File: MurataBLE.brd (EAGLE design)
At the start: 70 x 92 mm, 39 parts, among them CON1 C-2235, IC1 I-5448, IC3 74LVC1G00DBV, Q1 FC-135 32.7680KA-AG3, Q2 12MHz, SW1 P8073, SW2 P8073, SW3 P8073, U1 IC_BLE_LBCA2HNZYZ-711, X1 TSW-112-02-S-S

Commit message: [ USB ] lisence stated
CC-BY-SA
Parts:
- added TP5, TP6, TP7, TP8: TPTP06R, testpad_local:TP06R
- TP1, TP2, TP3, TP4: value TPTP07SQ -> TPTP06SQ; device testpad_local:TP07SQ -> testpad_local:TP06SQ
- moved TP1 0.30 mm to (42.2, 25.4)
- moved TP3 0.30 mm to (42.2, 26.7)
- moved TP2 0.20 mm to (43.0, 25.4)
- moved TP4 0.20 mm to (43.0, 26.7)
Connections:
- net P0_0: now also TP8.TP
- net P0_1: now also TP7.TP
- net TGT_RX: now also TP6.TP
- net TGT_TX: now also TP5.TP
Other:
- board text added: "CC-BY-SA Licensed"
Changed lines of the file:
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@@
 <wire x1="23.2" y1="28.8" x2="24.1" y2="28.8" width="0.15" layer="41"/>
 <wire x1="23.2" y1="27.6" x2="24.1" y2="27.6" width="0.15" layer="41"/>
+<text x="52.6" y="39.4" size="1" layer="16" ratio="20" rot="MR0">CC-BY-SA Licensed</text>
 </plain>
 <attributes>
@@
 <attribute name="VALUE" x="29.9" y="28.7" size="1" layer="27" ratio="20"/>
 </element>
-<element name="TP1" library="testpad_local" package="TP07SQ" value="TPTP07SQ" x="41.9" y="25.4" smashed="yes">
-<attribute name="TP_SIGNAL_NAME" value="" x="41.9" y="23.495" size="1" layer="37"/>
-<attribute name="VALUE" x="41.519" y="25.019" size="0.0254" layer="27"/>
-</element>
-<element name="TP2" library="testpad_local" package="TP07SQ" value="TPTP07SQ" x="42.8" y="25.4" smashed="yes">
-<attribute name="TP_SIGNAL_NAME" value="" x="42.8" y="23.495" size="1" layer="37"/>
-<attribute name="VALUE" x="42.419" y="25.019" size="0.0254" layer="27"/>
-</element>
-<element name="TP3" library="testpad_local" package="TP07SQ" value="TPTP07SQ" x="41.9" y="26.7" smashed="yes">
-<attribute name="TP_SIGNAL_NAME" value="" x="41.9" y="24.795" size="1" layer="37"/>
-<attribute name="VALUE" x="41.519" y="26.319" size="0.0254" layer="27"/>
-</element>
-<element name="TP4" library="testpad_local" package="TP07SQ" value="TPTP07SQ" x="42.8" y="26.7" smashed="yes">
-<attribute name="TP_SIGNAL_NAME" value="" x="42.8" y="24.795" size="1" layer="37"/>
-<attribute name="VALUE" x="42.419" y="26.319" size="0.0254" layer="27"/>
+<element name="TP1" library="testpad_local" package="TP06SQ" value="TPTP06SQ" x="42.2" y="25.4" smashed="yes">
+<attribute name="TP_SIGNAL_NAME" value="" x="42.2" y="23.495" size="1" layer="37"/>
+<attribute name="VALUE" x="41.819" y="25.019" size="0.0254" layer="27"/>
+</element>
+<element name="TP2" library="testpad_local" package="TP06SQ" value="TPTP06SQ" x="43" y="25.4" smashed="yes">
+<attribute name="TP_SIGNAL_NAME" value="" x="43" y="23.495" size="1" layer="37"/>
+<attribute name="VALUE" x="42.619" y="25.019" size="0.0254" layer="27"/>
+</element>
+<element name="TP3" library="testpad_local" package="TP06SQ" value="TPTP06SQ" x="42.2" y="26.7" smashed="yes">
+<attribute name="TP_SIGNAL_NAME" value="" x="42.2" y="24.795" size="1" layer="37"/>
+<attribute name="VALUE" x="41.819" y="26.319" size="0.0254" layer="27"/>
+</element>
+<element name="TP4" library="testpad_local" package="TP06SQ" value="TPTP06SQ" x="43" y="26.7" smashed="yes">
+<attribute name="TP_SIGNAL_NAME" value="" x="43" y="24.795" size="1" layer="37"/>
+<attribute name="VALUE" x="42.619" y="26.319" size="0.0254" layer="27"/>
 </element>
 <element name="R4" library="mylib" package="C0402" value="270/1005" x="32" y="27.3" smashed="yes" rot="R90">
@@
 <element name="LED1" library="mylib" package="LED_3SEG_SMD" value="LED_3SEG" x="22.4" y="35.8" smashed="yes">
 <attribute name="NAME" x="25.3" y="35.3" size="1" layer="25" ratio="20"/>
+</element>
+<element name="TP5" library="testpad_local" package="TP06R" value="TPTP06R" x="41.9" y="25.4" smashed="yes">
+<attribute name="TP_SIGNAL_NAME" value="" x="41.9" y="23.495" size="1" layer="37"/>
+<attribute name="VALUE" x="41.646" y="24.892" size="0.0254" layer="27"/>
+</element>
+<element name="TP6" library="testpad_local" package="TP06R" value="TPTP06R" x="41.9" y="26.7" smashed="yes">
+<attribute name="TP_SIGNAL_NAME" value="" x="41.9" y="24.795" size="1" layer="37"/>
+<attribute name="VALUE" x="41.646" y="26.192" size="0.0254" layer="27"/>
+</element>
+<element name="TP7" library="testpad_local" package="TP06R" value="TPTP06R" x="43.3" y="26.7" smashed="yes">
+<attribute name="TP_SIGNAL_NAME" value="" x="43.3" y="24.795" size="1" layer="37"/>
+<attribute name="VALUE" x="43.046" y="26.192" size="0.0254" layer="27"/>
+</element>
+<element name="TP8" library="testpad_local" package="TP06R" value="TPTP06R" x="43.3" y="25.4" smashed="yes">
+<attribute name="TP_SIGNAL_NAME" value="" x="43.3" y="23.495" size="1" layer="37"/>
+<attribute name="VALUE" x="43.046" y="24.892" size="0.0254" layer="27"/>
 </element>
 </elements>
@@
 <wire x1="48.7" y1="26" x2="48.7" y2="25.7" width="0.25" layer="1"/>
 <wire x1="48.7" y1="25.7" x2="45.8" y2="22.8" width="0.25" layer="1"/>
-<wire x1="43.7" y1="25.4" x2="44.3" y2="26" width="0.25" layer="1"/>
-<wire x1="44.3" y1="26" x2="48.7" y2="26" width="0.25" layer="1"/>
+<wire x1="44" y1="25.4" x2="44.6" y2="26" width="0.25" layer="1"/>
+<wire x1="44.6" y1="26" x2="48.7" y2="26" width="0.25" layer="1"/>
 <wire x1="45.8" y1="22.8" x2="45.8" y2="22.2" width="0.25" layer="1"/>
 <wire x1="33" y1="15.6" x2="39.2" y2="15.6" width="0.25" layer="1"/>
@@
 <wire x1="31.7" y1="14.3" x2="33" y2="15.6" width="0.25" layer="1"/>
 <contactref element="TP2" pad="TP"/>
-<wire x1="42.8" y1="25.4" x2="43.7" y2="25.4" width="0.25" layer="1"/>
+<contactref element="TP8" pad="TP"/>
+<wire x1="43" y1="25.4" x2="43.3" y2="25.4" width="0.25" layer="1"/>
+<wire x1="44" y1="25.4" x2="43.3" y2="25.4" width="0.25" layer="1"/>
 </signal>
 <signal name="P0_1">
@@
 <wire x1="31.4" y1="14.8" x2="32.7" y2="16.1" width="0.25" layer="1"/>
 <contactref element="TP4" pad="TP"/>
-<wire x1="48.7" y1="26.7" x2="42.8" y2="26.7" width="0.25" layer="1"/>
+<wire x1="48.7" y1="26.7" x2="43.3" y2="26.7" width="0.25" layer="1"/>
+<contactref element="TP7" pad="TP"/>
+<wire x1="43.3" y1="26.7" x2="43" y2="26.7" width="0.25" layer="1"/>
 </signal>
 <signal name="P0_2">
@@
 <wire x1="41.4" y1="23.7" x2="41.4" y2="24.9" width="0.25" layer="1"/>
 <contactref element="TP1" pad="TP"/>
-<wire x1="41.9" y1="25.4" x2="41.4" y2="24.9" width="0.25" layer="1"/>
+<contactref element="TP5" pad="TP"/>
+<wire x1="42.2" y1="25.4" x2="41.9" y2="25.4" width="0.25" layer="1"/>
+<wire x1="41.4" y1="24.9" x2="41.9" y2="25.4" width="0.25" layer="1"/>
 </signal>
 <signal name="TGT_RX">
@@
 <wire x1="40.25" y1="23.35" x2="40.9" y2="24" width="0.25" layer="1"/>
 <contactref element="TP3" pad="TP"/>
-<wire x1="41.9" y1="26.7" x2="40.9" y2="25.7" width="0.25" layer="1"/>
+<contactref element="TP6" pad="TP"/>
+<wire x1="42.2" y1="26.7" x2="41.9" y2="26.7" width="0.25" layer="1"/>
+<wire x1="40.9" y1="25.7" x2="41.9" y2="26.7" width="0.25" layer="1"/>
 </signal>
 <signal name="N$4">

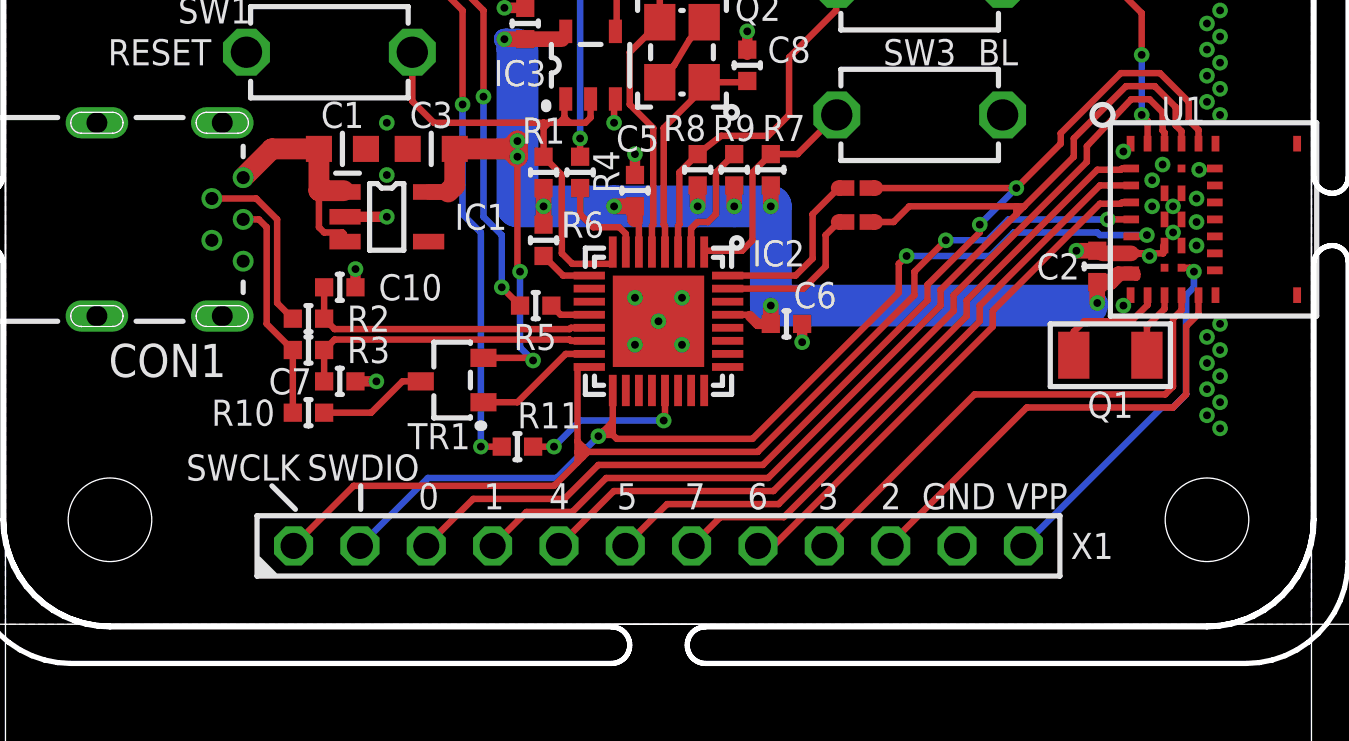
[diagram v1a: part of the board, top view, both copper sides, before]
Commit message: [ USB ] extend pin header X1
now ALL pins on header
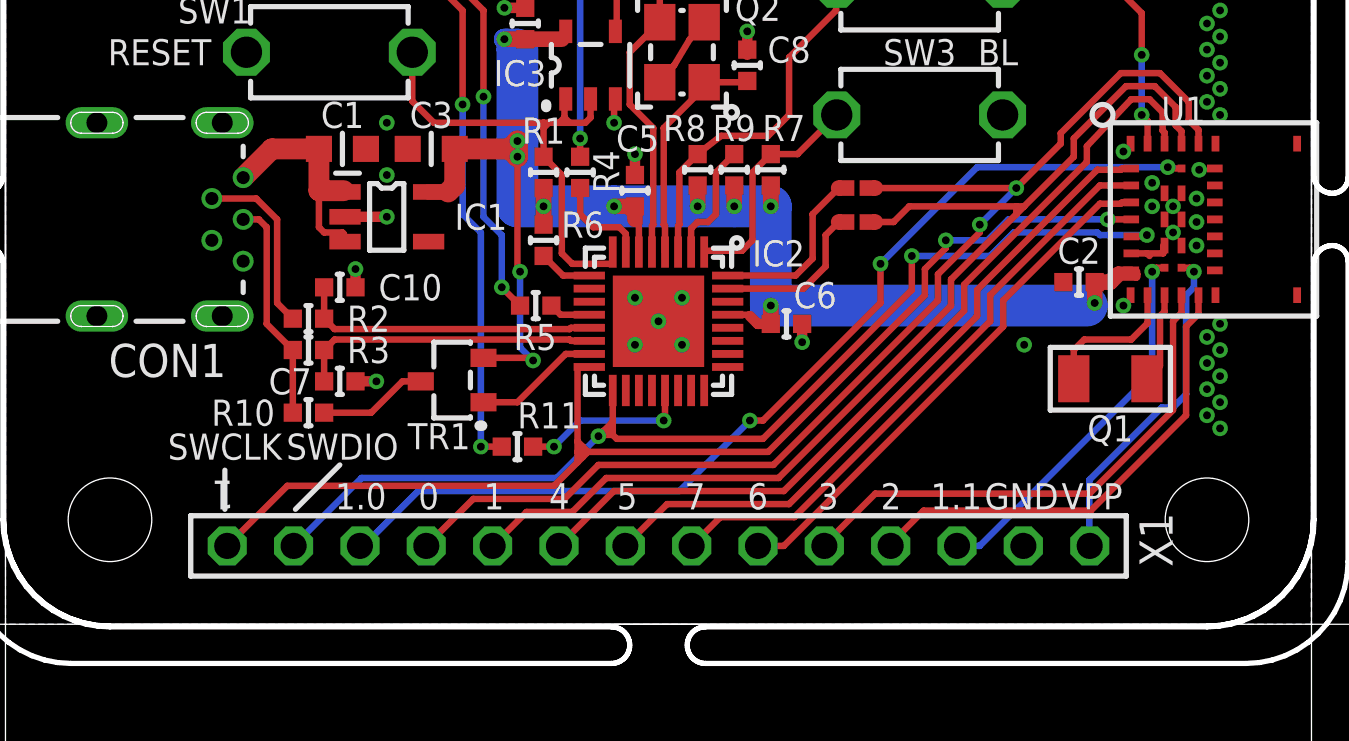
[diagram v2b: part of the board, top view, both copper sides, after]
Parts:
- X1: value TSW-112-02-S-S -> TSW-114-02-S-S; device con-samtec.local:TSW-112-02-S-S -> con-samtec.local:TSW-114-02-S-S
- moved C2 0.92 mm to (51.1, 23.1), turned to 180 degrees
- moved Q1 0.90 mm to (52.3, 19.4)
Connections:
- net GND: now also X1.13; no longer X1.11
- net P0_0: now also X1.5; no longer X1.4
- net P0_1: now also X1.4; no longer X1.3
- net P0_2: now also X1.11; no longer X1.10
- net P0_3: now also X1.10; no longer X1.9
- net P0_4: now also X1.6; no longer X1.5
- net P0_5: now also X1.7; no longer X1.6
- net P0_6: now also X1.9; no longer X1.8
- net P0_7: now also X1.8; no longer X1.7
- net P1_0: now also X1.3
- net P1_1: now also X1.12
- net VPP: now also X1.14; no longer X1.12
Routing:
- net P1_0: track 0.00 -> 38.4 mm, vias 0 -> 3
- net P1_1: track 0.00 -> 14.6 mm, vias 0 -> 1
- net SWCLK: track 43.2 -> 46.0 mm
- net SWDIO: track 39.5 -> 42.2 mm
- net GND: track 24.2 -> 21.7 mm, vias 48 -> 46
- net VPP: track 14.0 -> 13.0 mm
- net N$2: track 4.52 -> 5.42 mm
- net N$3: track 2.58 -> 3.48 mm
- net P0_3: track 19.5 -> 20.1 mm
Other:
- board text added: "1.0"
- board text added: "1.1"

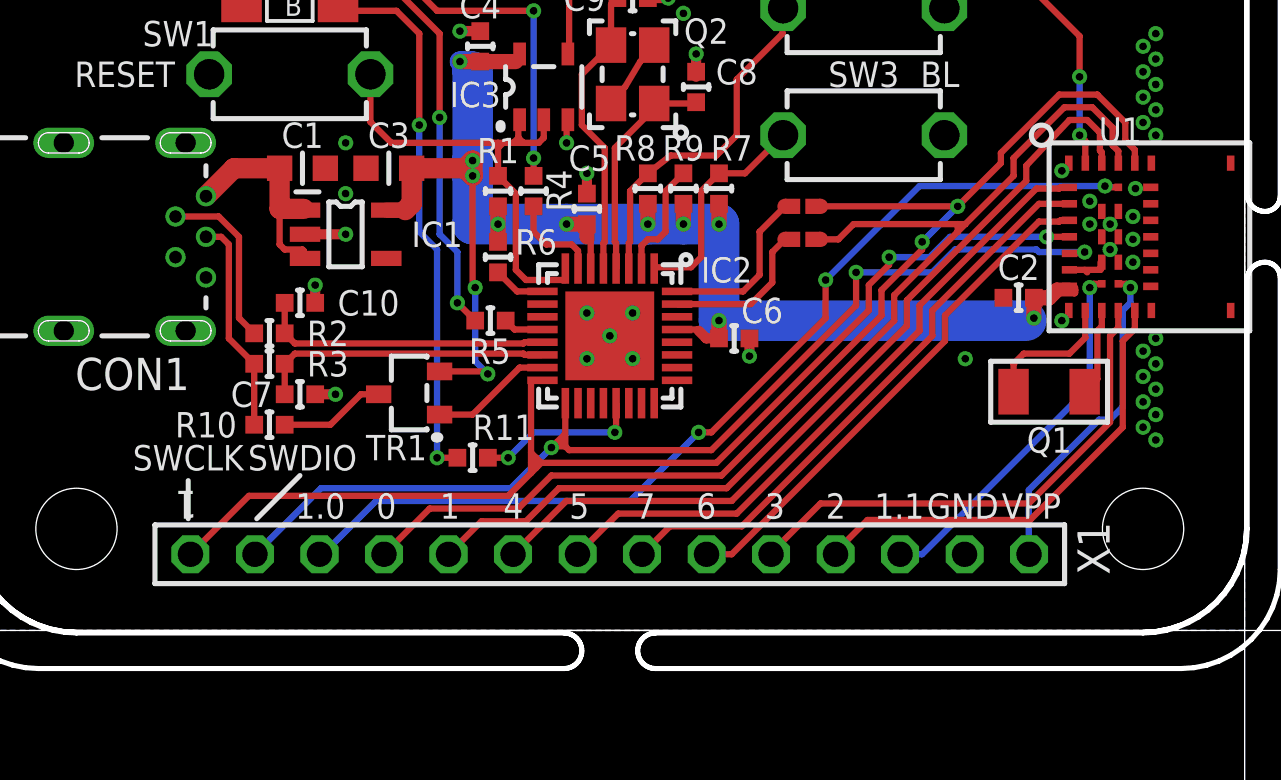
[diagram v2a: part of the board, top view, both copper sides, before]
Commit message: [ USB ] update as library
TP
X1 Pin header
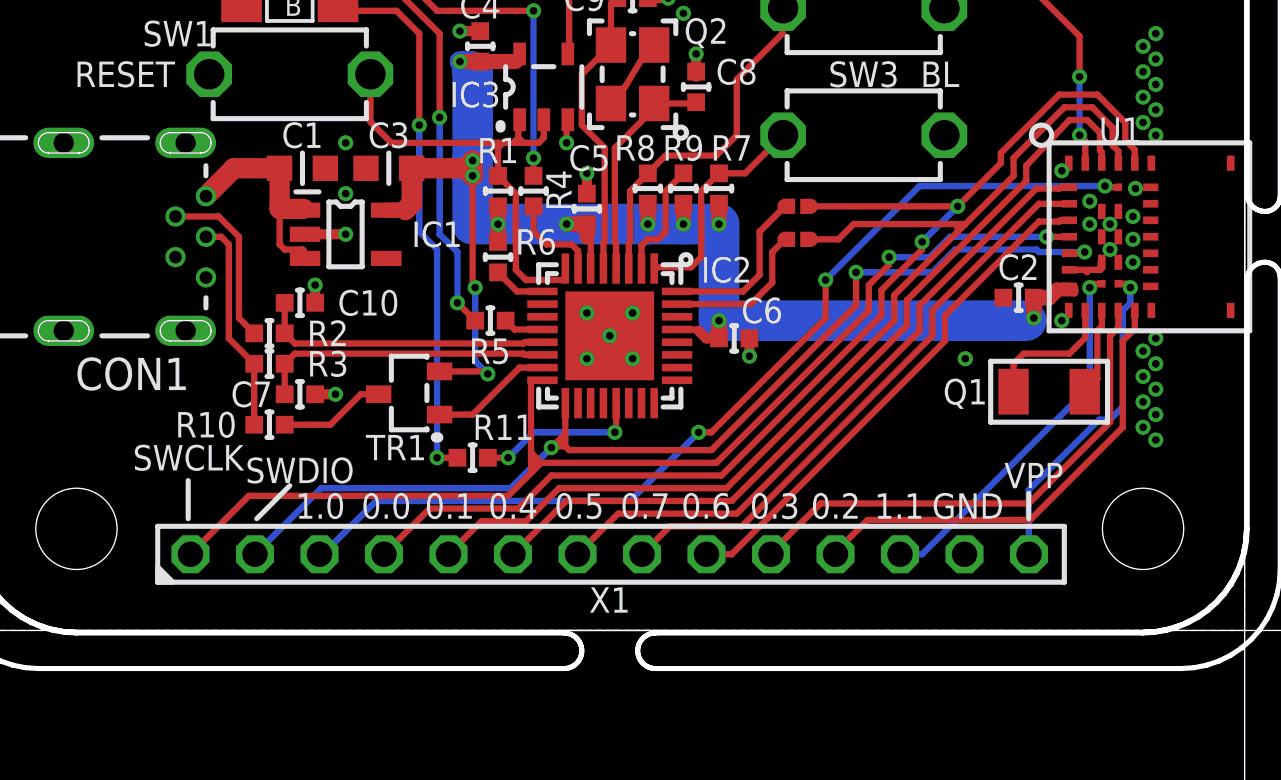
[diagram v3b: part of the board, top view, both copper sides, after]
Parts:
- TP1, TP2, TP3, TP4: value TPTP06SQ -> TESTPAD; device testpad_local:TP06SQ -> mylib:TP06RECT
- X1: device con-samtec.local:TSW-114-02-S-S -> mylib:TSW-114-02-S-S
- moved TP2 1.58 mm to (42.1, 26.7)
- moved TP3 1.39 mm to (42.7, 25.4)
- moved TP7 0.40 mm to (42.9, 26.7)
- moved TP8 0.40 mm to (42.9, 25.4)
- moved TP4 0.30 mm to (42.7, 26.7)
- moved TP1 0.10 mm to (42.1, 25.4)
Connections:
- net P0_0: now also TP3.TP; no longer TP2.TP
- net TGT_RX: now also TP2.TP; no longer TP3.TP
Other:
- board text added: "0.0"
- board text added: "0.1"
- board text added: "0.2"
- board text added: "0.3"
- board text added: "0.4"
- board text added: "0.5"
- board text added: "0.6"
- board text added: "0.7"
- board text removed: "0"
- board text removed: "1"
- board text removed: "2"
- board text removed: "3"
- board text removed: "4"
- board text removed: "5"
- board text removed: "6"
- board text removed: "7"

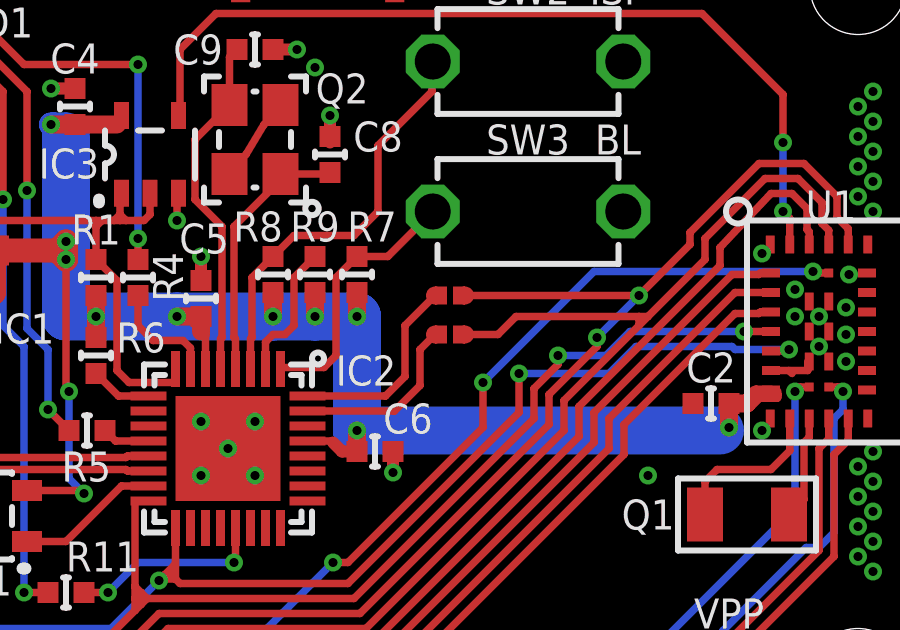
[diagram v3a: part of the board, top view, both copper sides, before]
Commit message: [ USB ][ BRD ] add jumpers
added jumpers to keep net name on schematic
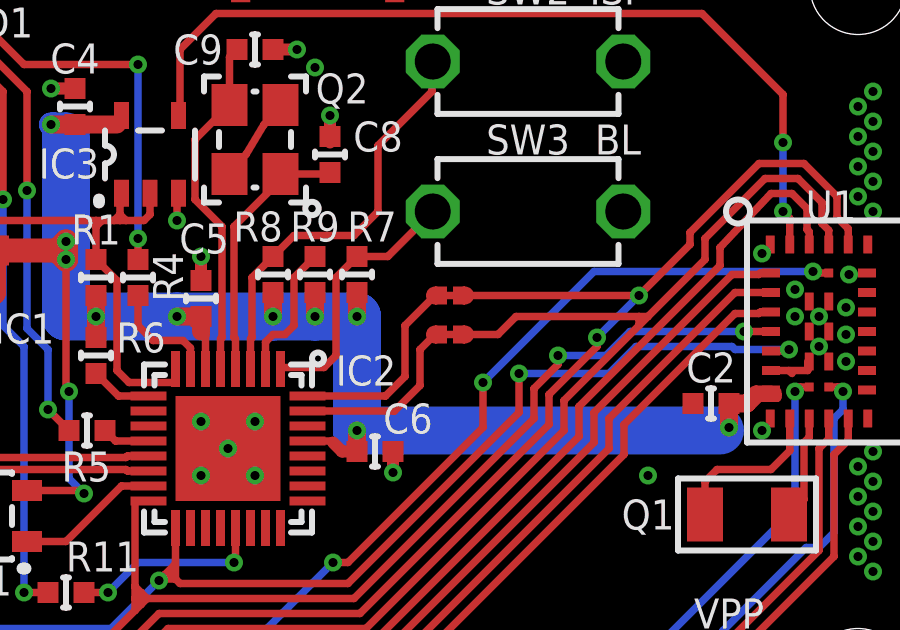
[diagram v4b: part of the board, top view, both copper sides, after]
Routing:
- net N$15: track 0.00 -> 0.60 mm
- net N$14: track 0.00 -> 0.60 mm
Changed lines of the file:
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@@
 <wire x1="28.2" y1="16.8" x2="28.2" y2="25" width="0.25" layer="16"/>
+</signal>
+<signal name="N$14">
+<wire x1="42.1" y1="26.7" x2="42.7" y2="26.7" width="0.25" layer="1"/>
+</signal>
+<signal name="N$15">
+<wire x1="42.1" y1="25.4" x2="42.7" y2="25.4" width="0.25" layer="1"/>
 </signal>
 </signals>
